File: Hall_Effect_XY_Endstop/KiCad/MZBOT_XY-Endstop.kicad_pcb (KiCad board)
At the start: 2 copper layers, 56 x 18 mm, 26 parts, among them J1 CONN_01X04, U1 SS49E, U2 SS49E, U3 LM393, U4 AP2210N

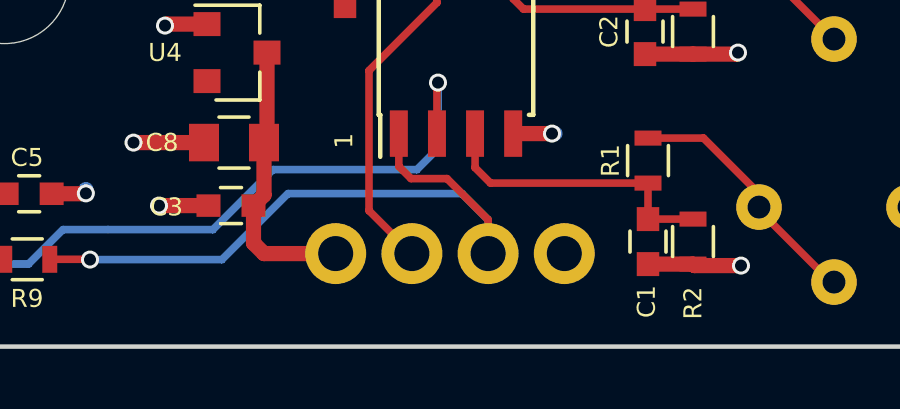
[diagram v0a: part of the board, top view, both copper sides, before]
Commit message: Add silkscreen to Output Connector
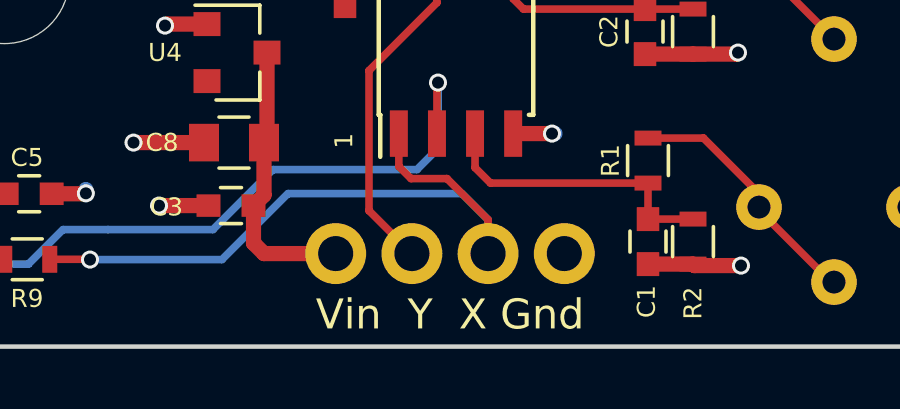
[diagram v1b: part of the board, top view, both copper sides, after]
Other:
- board text added: "Gnd X Y Vin"
- board text added: "Vin Y X Gnd"
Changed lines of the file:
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@@
-(kicad_pcb (version 20171130) (host pcbnew "(5.0.0-3-g5ebb6b6)")
+(kicad_pcb (version 20171130) (host pcbnew "(5.1.5)-3")
   (general
     (thickness 1.6)
-    (drawings 28)
+    (drawings 30)
     (tracks 121)
     (zones 0)
@@
   )
   (layers
-    (0 F.Cu signal)
-    (31 B.Cu signal hide)
+    (0 F.Cu signal hide)
+    (31 B.Cu signal)
     (32 B.Adhes user)
-    (33 F.Adhes user)
+    (33 F.Adhes user hide)
     (34 B.Paste user)
     (35 F.Paste user hide)
     (36 B.SilkS user)
-    (37 F.SilkS user)
+    (37 F.SilkS user hide)
     (38 B.Mask user)
-    (39 F.Mask user)
-    (40 Dwgs.User user)
+    (39 F.Mask user hide)
+    (40 Dwgs.User user hide)
     (41 Cmts.User user)
     (42 Eco1.User user)
@@
     (zone_45_only no)
     (trace_min 0.2)
-    (segment_width 0.2)
-    (edge_width 0.15)
     (via_size 0.6)
     (via_drill 0.4)
@@
     (uvia_min_size 0.2)
     (uvia_min_drill 0.1)
+    (edge_width 0.15)
+    (segment_width 0.2)
     (pcb_text_width 0.3)
     (pcb_text_size 1.5 1.5)
@@
     (pad_to_mask_clearance 0.2)
     (aux_axis_origin 0 0)
-    (visible_elements 7FFEFFFF)
+    (grid_origin 142.6 107.9)
+    (visible_elements 7FFFFFFF)
     (pcbplotparams
       (layerselection 0x010f0_ffffffff)
@@
       (xy 0.011887 1.460649)) (layer B.SilkS) (width 0.01))
   )
+  (gr_text "Vin  Y  X Gnd" (at 142.6 109.932) (layer F.SilkS)
+    (effects (font (size 1 1) (thickness 0.15)))
+  )
+  (gr_text "Gnd X  Y  Vin" (at 142.6 109.932) (layer B.SilkS)
+    (effects (font (size 1 1) (thickness 0.15)) (justify mirror))
+  )
   (gr_text 1 (at 139.065 104.14 90) (layer F.SilkS)
     (effects (font (size 0.6 0.6) (thickness 0.15)))
@@
     (effects (font (size 1.5 1.5) (thickness 0.3)))
   )
-  (gr_text BOT (at 134.35 98.9 270) (layer B.SilkS)
+  (gr_text BOT (at 134.35 98.9 270) (layer B.Fab)
     (effects (font (size 1.2 1.1) (thickness 0.14)) (justify mirror))
   )
-  (gr_text MZ (at 134.35 101.55 270) (layer B.SilkS)
+  (gr_text MZ (at 134.35 101.55 270) (layer B.Fab)
     (effects (font (size 1.1 1.1) (thickness 0.25)) (justify mirror))
   )
